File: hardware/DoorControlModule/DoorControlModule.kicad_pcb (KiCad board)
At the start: 6 copper layers, 68 x 65 mm, 135 parts, among them IC1 CY8C4147AZE-S475, IC2 TLS850B0TBV33ATMA1, IC3 MAX6818, IC4 TJA1043T,118, IC5 LM2901BYPT, IC6 BTS72002EPAXUMA1, IC7 LM74610, J1 64334-0100, J2 501331-0507, Q1 VOMA618A-4X001T, Q2 VOMA618A-4X001T, Q3 IPD50N04S4L08ATMA1, U1 BTM9021EP, U2 BTM9021EP, U3 BTM9021EP, U4 BTN70301EPAXUMA1, U5 BTN70301EPAXUMA1, U6 BTN70301EPAXUMA1, U7 BTN9990LV, U8 BTN9990LV, Y1 CX3225CA24000D0HSSCC, Y2 NX3215SA-32.768K-STD-MUS-2

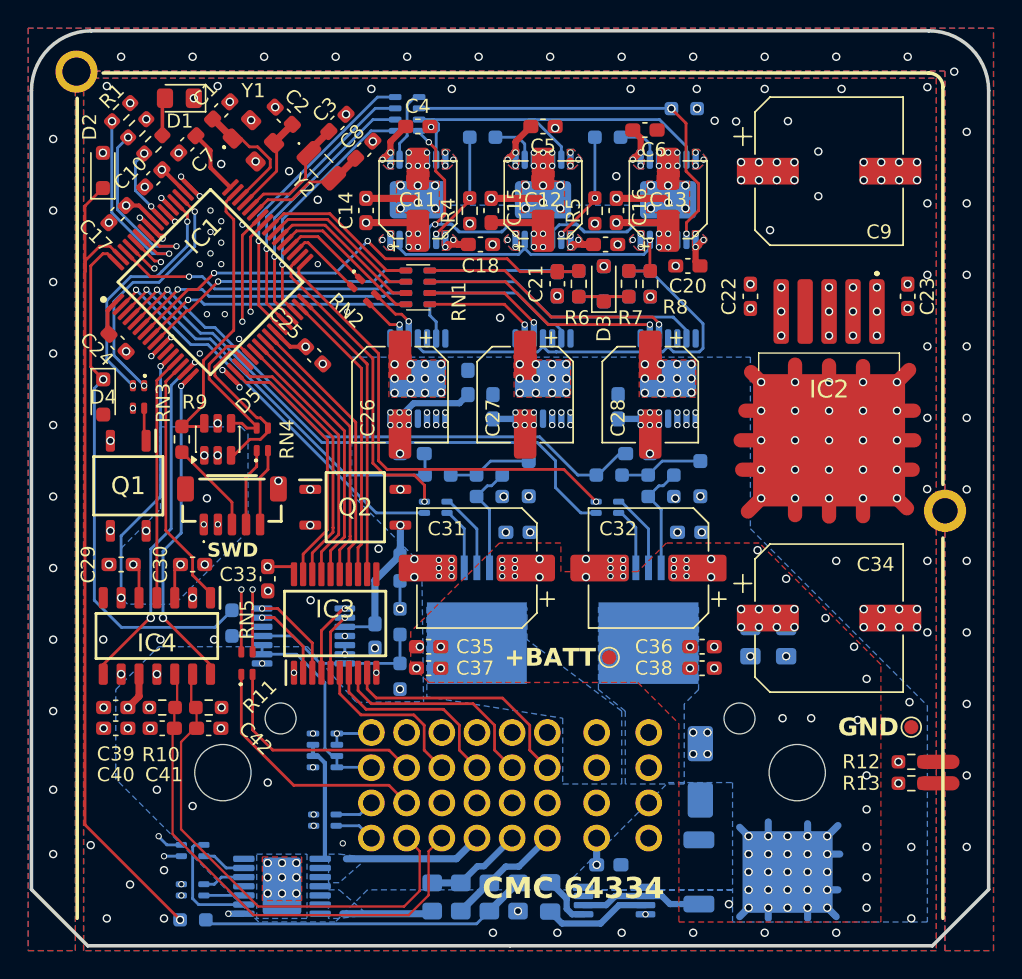
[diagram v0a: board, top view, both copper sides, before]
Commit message: top silkscreen cleanup, GND test-point removed
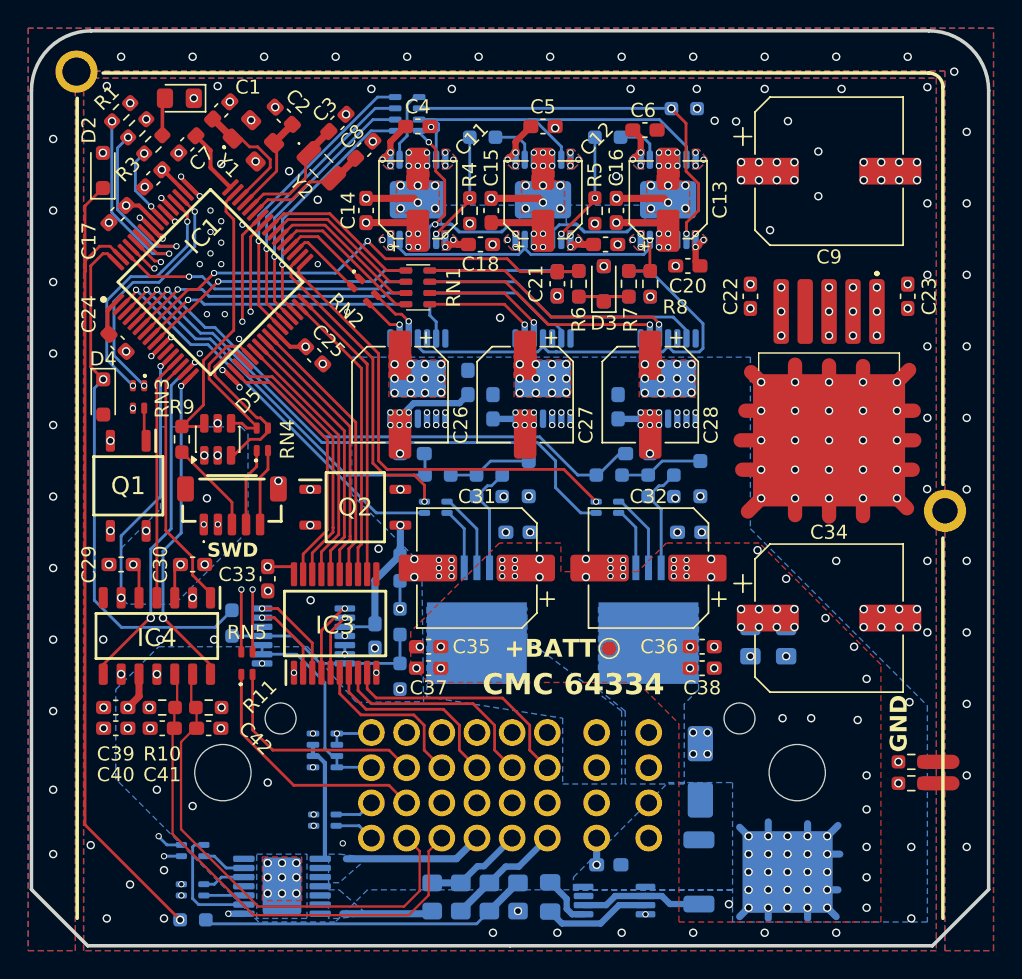
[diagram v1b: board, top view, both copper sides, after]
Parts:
- removed TP2: TestPoint, TestPoint:TestPoint_Pad_D1.0mm
- moved TP1 0.64 mm to (143.9, 95.6)
